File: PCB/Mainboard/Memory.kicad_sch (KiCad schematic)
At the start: 10 parts, among them J301 Conn_SIMM72, J302 Conn_SIMM72, U301 74F541, U302 74F541

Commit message: Add files via upload
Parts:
- removed J301, J302: Conn_SIMM72, My_Components:Conn_SIMM72, symbol my_components:Conn_SIMM72
- removed R72: 22, Resistor_SMD:R_0612_1632Metric_Pad1.18x3.40mm_HandSolder, symbol Device:R
- removed RN301, RN302, RN303, RN304, RN305: 22, Resistor_THT:R_Array_SIP8, symbol Device:R_Pack04
- removed U301, U302: 74F541, My_Components:IC_DIP20_300, symbol 74xx:74LS541
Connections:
- no-connect marks 18 -> 0
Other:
- note removed: "DRAM Bank 0/1"
- note removed: "DRAM Bank 2/3"

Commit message: Add files via upload
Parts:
- added C101: 180nF, symbol PCM_Elektuur:C
- added C95: 150nF, symbol PCM_Elektuur:C
- added J15: RAM Module, symbol PC110:RAM_MOD
- added U28, U33: M5M4V16160, symbol PC110:M5M4V16160
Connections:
- new net GND: C101.2 (-), C95.2 (-), J15.10 (GND), J15.27 (GND), J15.36 (GND), J15.55 (GND), U28.26 (GND), U28.45 (GND), U28.50 (GND), U33.26 (GND), U33.45 (GND), U33.50 (GND)
- new net PNET1: C101.1 (+), C95.1 (+), J15.14 (VCC), J15.21 (VCC), J15.5 (VCC), U28.1 (VCC), U28.25 (VCC), U28.6 (VCC), U33.1 (VCC), U33.25 (VCC), U33.6 (VCC)
- no-connect marks 0 -> 10

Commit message: Add files via upload
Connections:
- net CPU_D0: now reaches J15.1 (D0)
- net CPU_D0: now also U28.2 (DQ0)
- net RAM_A11: now reaches J15.15 (A11)
- net RAM_A11: now also U28.19 (A11), U33.19 (A11)
- net RAM_A10: now reaches J15.16 (A10)
- net RAM_A10: now also U28.20 (A10), U33.20 (A10)
- net RAM_A0: now reaches J15.17 (A0)
- net RAM_A0: now also U28.21 (A0), U33.21 (A0)
- net RAM_A1: now reaches J15.18 (A1)
- net RAM_A1: now also U28.22 (A1), U33.22 (A1)
- net RAM_A2: now reaches J15.19 (A2)
- net RAM_A2: now also U28.23 (A2), U33.23 (A2)
- net CPU_D1: now reaches J15.2 (D1)
- net CPU_D1: now also U28.3 (DQ1)
- net RAM_A3: now reaches J15.20 (A3)
- net RAM_A3: now also U28.24 (A3), U33.24 (A3)
- net CPU_D16: now reaches J15.22 (D16)
- net CPU_D16: now also U33.2 (DQ0)
- net CPU_D17: now reaches J15.23 (D17)
- net CPU_D17: now also U33.3 (DQ1)
- net CPU_D18: now reaches J15.24 (D18)
- net CPU_D18: now also U33.4 (DQ2)
- net CPU_D19: now reaches J15.25 (D19)
- net CPU_D19: now also U33.5 (DQ3)
- net CPU_D21: now reaches J15.28 (D21)
- net CPU_D21: now also U33.8 (DQ5)
- net CPU_D22: now reaches J15.29 (D22)
- net CPU_D22: now also U33.9 (DQ6)
- net CPU_D2: now reaches J15.3 (D2)
- net CPU_D2: now also U28.4 (DQ2)
- net CPU_D23: now reaches J15.30 (D23)
- net CPU_D23: now also U33.10 (DQ7)
- net CPU_D24: now reaches J15.32 (D24)
- net CPU_D24: now also U33.41 (DQ8)
- net CPU_D25: now reaches J15.33 (D25)
- net CPU_D25: now also U33.42 (DQ9)
- net CPU_D26: now reaches J15.34 (D26)
- net CPU_D26: now also U33.43 (DQ10)
- net CPU_D27: now reaches J15.35 (D27)
- net CPU_D27: now also U33.44 (DQ11)
- net CPU_D28: now reaches J15.37 (D28)
- net CPU_D28: now also U33.46 (DQ12)
- net CPU_D29: now reaches J15.38 (D29)
- net CPU_D29: now also U33.47 (DQ13)
- net CPU_D30: now reaches J15.39 (D30)
- net CPU_D30: now also U33.48 (DQ14)
- net CPU_D3: now reaches J15.4 (D3)
- net CPU_D3: now also U28.5 (DQ3)
- net CPU_D31: now reaches J15.40 (D31)
- net CPU_D31: now also U33.49 (DQ15)
- net RAM_A4: now reaches J15.41 (A4)
- net RAM_A4: now also U28.27 (A4), U33.27 (A4)
- net RAM_A5: now reaches J15.42 (A5)
- net RAM_A5: now also U28.28 (A5), U33.28 (A5)
- net RAM_A6: now reaches J15.43 (A6)
- net RAM_A6: now also U28.29 (A6), U33.29 (A6)
- net RAM_A7: now reaches J15.44 (A7)
- net RAM_A7: now also U28.30 (A7), U33.30 (A7)
- net RAM_A8: now reaches J15.45 (A8)
- net RAM_A8: now also U28.31 (A8), U33.31 (A8)
- net RAM_A9: now reaches J15.46 (A9)
- net RAM_A9: now also U28.32 (A9), U33.32 (A9)
- net CPU_D8: now reaches J15.51 (D8)
- net CPU_D8: now also U28.41 (DQ8)
- net CPU_D9: now reaches J15.52 (D9)
- net CPU_D9: now also U28.42 (DQ9)
- net CPU_D10: now reaches J15.53 (D10)
- net CPU_D10: now also U28.43 (DQ10)
- net CPU_D11: now reaches J15.54 (D11)
- net CPU_D11: now also U28.44 (DQ11)
- net CPU_D12: now reaches J15.56 (D12)
- net CPU_D12: now also U28.46 (DQ12)
- net CPU_D13: now reaches J15.57 (D13)
- net CPU_D13: now also U28.47 (DQ13)
- net CPU_D14: now reaches J15.58 (D14)
- net CPU_D14: now also U28.48 (DQ14)
- net CPU_D15: now reaches J15.59 (D15)
- net CPU_D15: now also U28.49 (DQ15)
- net CPU_D4: now reaches J15.6 (D4)
- net CPU_D4: now also U28.7 (DQ4)
- net CPU_D5: now reaches J15.7 (D5)
- net CPU_D5: now also U28.8 (DQ5)
- net CPU_D6: now reaches J15.8 (D6)
- net CPU_D6: now also U28.9 (DQ6)
- net CPU_D7: now reaches J15.9 (D7)
- net CPU_D7: now also U28.10 (DQ7)
- net CPU_D20: now reaches U33.7 (DQ4)
- net CPU_D20: now also J15.27 (GND)
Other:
- moved on the sheet: C101, C95, J15, U28, U33

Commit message: Add files via upload
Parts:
- added R101, R103, R106, R154, R159, R261, R272, R274: 33, symbol Device:R
- added R102, R105, R148, R158, R94: 470k, symbol Device:R
- added RA5: 470k, symbol Device:R_Pack04
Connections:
- net CPU_D10: now also U28.37 (DQ10); no longer U28.43 (DQ10)
- net CPU_D11: now also U28.38 (DQ11); no longer U28.44 (DQ11)
- net CPU_D12: now also U28.40 (DQ12); no longer U28.46 (DQ12)
- net CPU_D13: now also U28.41 (DQ13); no longer U28.47 (DQ13)
- net CPU_D14: now also U28.42 (DQ14); no longer U28.48 (DQ14)
- net CPU_D15: now also U28.43 (DQ15); no longer U28.49 (DQ15)
- net CPU_D24: now also U33.35 (DQ8); no longer U33.41 (DQ8)
- net CPU_D25: now also U33.36 (DQ9); no longer U33.42 (DQ9)
- net CPU_D26: now also U33.37 (DQ10); no longer U33.43 (DQ10)
- net CPU_D27: now also U33.38 (DQ11); no longer U33.44 (DQ11)
- net CPU_D28: now also U33.40 (DQ12); no longer U33.46 (DQ12)
- net CPU_D29: now also U33.41 (DQ13); no longer U33.47 (DQ13)
- net CPU_D30: now also U33.42 (DQ14); no longer U33.48 (DQ14)
- net CPU_D31: now also U33.43 (DQ15); no longer U33.49 (DQ15)
- net CPU_D8: now also U28.35 (DQ8); no longer U28.41 (DQ8)
- net CPU_D9: now also U28.36 (DQ9); no longer U28.42 (DQ9)
- net GND: now also U28.23 (GND), U28.30 (OE#), U28.39 (GND), U28.44 (GND), U33.23 (GND), U33.30 (OE#), U33.39 (GND), U33.44 (GND); no longer U28.26 (GND), U28.45 (GND), U28.50 (GND), U33.26 (GND), U33.45 (GND), U33.50 (GND)
- net PNET1: now also U28.22 (VCC), U33.22 (VCC), R102.2, R105.2, R148.2, R158.2, R94.2, RA5.5 (R4.2), RA5.6 (R3.2), RA5.7 (R2.2), RA5.8 (R1.2); no longer U28.25 (VCC), U33.25 (VCC)
- net RAM_A0: now also U28.18 (A0), U33.18 (A0); no longer U28.21 (A0), U33.21 (A0)
- net RAM_A1: now also U28.19 (A1), U33.19 (A1); no longer U28.22 (A1), U33.22 (A1)
- net RAM_A10: now also U28.17 (A10), U33.17 (A10); no longer U28.20 (A10), U33.20 (A10)
- net RAM_A11: now also U28.16 (A11), U33.16 (A11); no longer U28.19 (A11), U33.19 (A11)
- net RAM_A2: now also U28.20 (A2), U33.20 (A2); no longer U28.23 (A2), U33.23 (A2)
- net RAM_A3: now also U28.21 (A3), U33.21 (A3); no longer U28.24 (A3), U33.24 (A3)
- net RAM_A4: now also U28.24 (A4), U33.24 (A4); no longer U28.27 (A4), U33.27 (A4)
- net RAM_A5: now also U28.25 (A5), U33.25 (A5); no longer U28.28 (A5), U33.28 (A5)
- net RAM_A6: now also U28.26 (A6), U33.26 (A6); no longer U28.29 (A6), U33.29 (A6)
- net RAM_A7: now also U28.27 (A7), U33.27 (A7); no longer U28.30 (A7), U33.30 (A7)
- net RAM_A8: now also U28.28 (A8), U33.28 (A8); no longer U28.31 (A8), U33.31 (A8)
- net RAM_A9: now also U28.29 (A9), U33.29 (A9); no longer U28.32 (A9), U33.32 (A9)
- net at J15.11 (RAS2): now also R102.1, R103.2
- net LCASU#: now reaches J15.12 (LCASU#)
- net LCASU#: now also U28.32 (LCAS#), R274.2, RA5.4 (R4.1)
- net UCASU#: now reaches J15.13 (UCASU#)
- net UCASU#: now also U28.31 (UCAS#), R261.2, RA5.3 (R3.1)
- net RAM_ID1: now reaches J15.31 (ID1)
- net RAM_ID1: now also R148.1
- net UCASL#: now reaches J15.47 (UCASL#)
- net UCASL#: now also U33.31 (UCAS#), R159.2, RA5.1 (R1.1)
- net LCASL#: now reaches J15.48 (LCASL#)
- net LCASL#: now also U33.32 (LCAS#), R272.2, RA5.2 (R2.1)
- net at J15.49 (RAS3): now also R106.2, R94.1
- net RAMWE#: now reaches J15.50 (WE#)
- net RAMWE#: now also U28.14 (W#), U33.14 (W#), R154.2
- net RAM_ID0: now reaches J15.60 (ID0)
- net RAM_ID0: now also R158.1
- net at U33.15 (RAS#): now also U28.15 (RAS#), R101.2, R105.1
- new net RAM_LCASL#: R272.1
- new net RAM_LCASU#: R274.1
- new net RAM_RAMWE#: R154.1
- new net RAM_RAS1: R101.1
- new net RAM_RAS2: R103.1
- new net RAM_RAS3: R106.1
- new net RAM_UCASL#: R159.1
- new net RAM_UCASU#: R261.1
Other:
- moved on the sheet: C101, C95, J15, U28, U33

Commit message: Add files via upload
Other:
- company: (none) -> Recreated by: Ahmad Byagowi
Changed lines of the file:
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@@
 	(title_block
 		(title "PC110")
+		(company "Recreated by: Ahmad Byagowi")
 	)
 	(junction

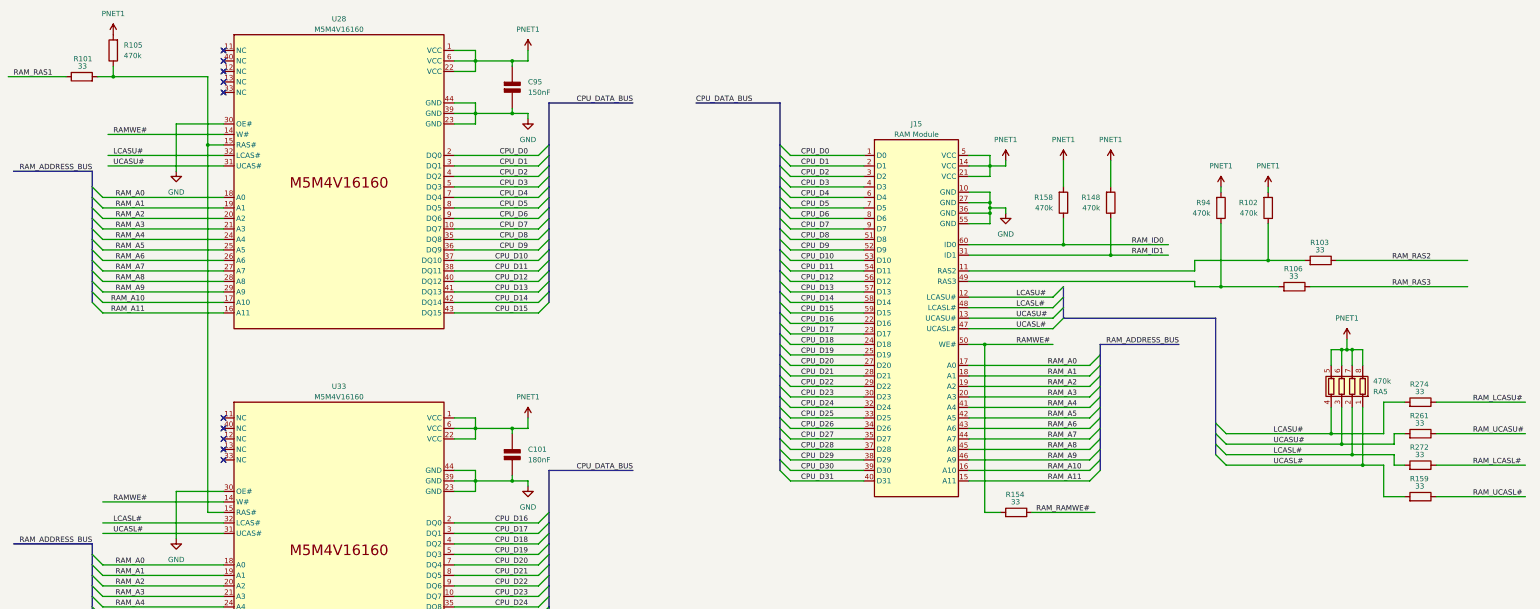
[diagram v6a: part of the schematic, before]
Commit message: Add part numbers to some SMT parts
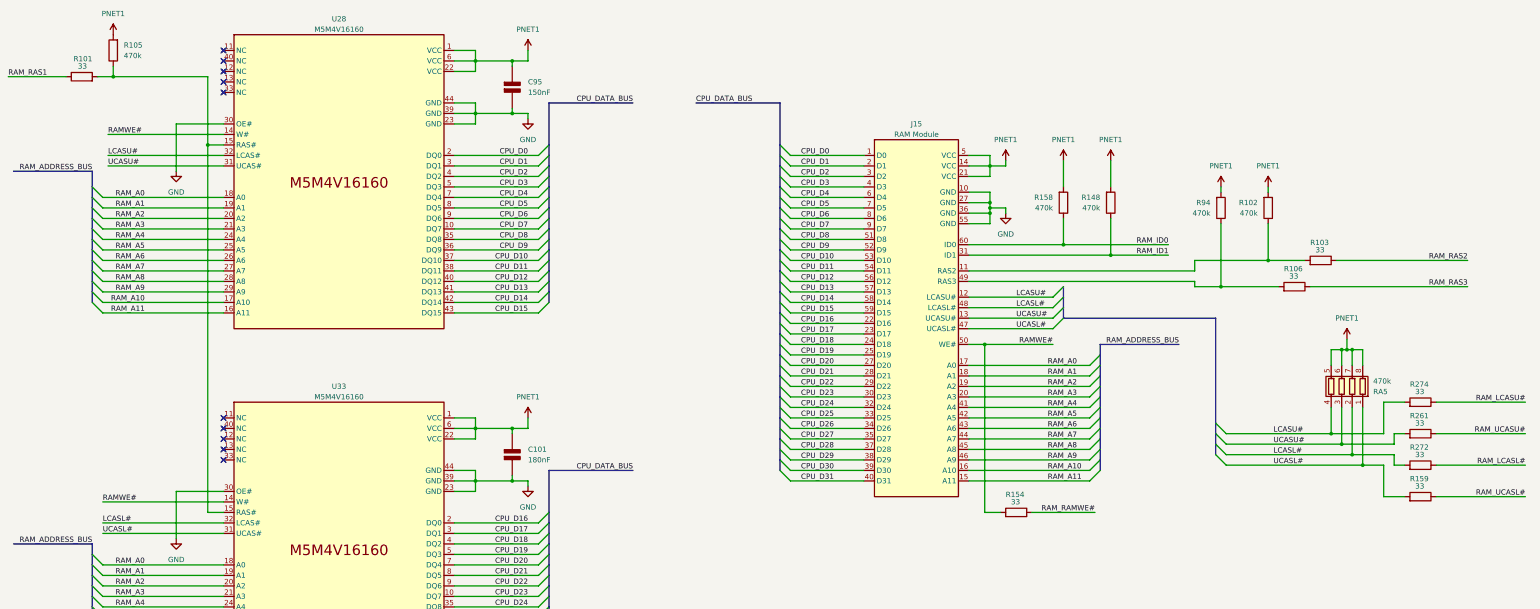
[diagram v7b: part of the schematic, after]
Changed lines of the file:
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@@
 	)
 	(label "LCASU#"
-		(at 57.15 93.98 0)
+		(at 55.88 93.98 0)
 		(effects
 			(font
@@
 	)
 	(label "RAM_ID0"
-		(at 303.53 115.57 0)
-		(effects
-			(font
-				(size 1.27 1.27)
-			)
-			(justify left bottom)
+		(at 312.42 115.57 180)
+		(effects
+			(font
+				(size 1.27 1.27)
+			)
+			(justify right bottom)
 		)
 	)
@@
 	)
 	(label "RAM_RAS1"
-		(at 33.02 74.93 0)
+		(at 31.75 74.93 0)
 		(effects
 			(font
@@
 	)
 	(label "RAM_LCASL#"
-		(at 386.08 168.91 0)
-		(effects
-			(font
-				(size 1.27 1.27)
-			)
-			(justify left bottom)
+		(at 398.78 168.91 180)
+		(effects
+			(font
+				(size 1.27 1.27)
+			)
+			(justify right bottom)
 		)
 	)
@@
 	)
 	(label "RAMWE#"
-		(at 57.15 177.8 0)
+		(at 54.61 177.8 0)
 		(effects
 			(font
@@
 	)
 	(label "RAM_RAMWE#"
-		(at 293.37 180.34 180)
+		(at 294.64 180.34 180)
 		(effects
 			(font
@@
 	)
 	(label "LCASL#"
-		(at 57.15 182.88 0)
+		(at 54.61 182.88 0)
 		(effects
 			(font
@@
 	)
 	(label "RAM_RAS2"
-		(at 375.92 119.38 180)
+		(at 384.81 119.38 180)
 		(effects
 			(font
@@
 	)
 	(label "RAM_UCASL#"
-		(at 386.08 176.53 0)
-		(effects
-			(font
-				(size 1.27 1.27)
-			)
-			(justify left bottom)
+		(at 398.78 176.53 180)
+		(effects
+			(font
+				(size 1.27 1.27)
+			)
+			(justify right bottom)
 		)
 	)
@@
 	)
 	(label "RAM_RAS3"
-		(at 375.92 125.73 180)
+		(at 384.81 125.73 180)
 		(effects
 			(font
@@
 	)
 	(label "UCASU#"
-		(at 57.15 96.52 0)
+		(at 55.88 96.52 0)
 		(effects
 			(font
@@
 	)
 	(label "RAMWE#"
-		(at 275.59 139.7 0)
-		(effects
-			(font
-				(size 1.27 1.27)
-			)
-			(justify left bottom)
+		(at 284.48 139.7 180)
+		(effects
+			(font
+				(size 1.27 1.27)
+			)
+			(justify right bottom)
 		)
 	)
 	(label "RAM_ID1"
-		(at 303.53 118.11 0)
-		(effects
-			(font
-				(size 1.27 1.27)
-			)
-			(justify left bottom)
+		(at 312.42 118.11 180)
+		(effects
+			(font
+				(size 1.27 1.27)
+			)
+			(justify right bottom)
 		)
 	)
@@
 	)
 	(label "UCASL#"
-		(at 57.15 185.42 0)
+		(at 54.61 185.42 0)
 		(effects
 			(font
@@
 	)
 	(label "RAMWE#"
-		(at 57.15 88.9 0)
+		(at 55.88 88.9 0)
 		(effects
 			(font
@@
 	)
 	(label "RAM_LCASU#"
-		(at 386.08 153.67 0)
-		(effects
-			(font
-				(size 1.27 1.27)
-			)
-			(justify left bottom)
+		(at 398.78 153.67 180)
+		(effects
+			(font
+				(size 1.27 1.27)
+			)
+			(justify right bottom)
 		)
 	)
@@
 	)
 	(label "RAM_UCASU#"
-		(at 386.08 161.29 0)
-		(effects
-			(font
-				(size 1.27 1.27)
-			)
-			(justify left bottom)
-		)
-	)
+		(at 398.78 161.29 180)
+		(effects
+			(font
+				(size 1.27 1.27)
+			)
+			(justify right bottom)
+		)
+	)

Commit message: Add files via upload
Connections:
- net RAM_RAS1 renamed RAM_RAS0
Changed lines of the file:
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@@
 		)
 	)
-	(label "RAM_RAS1"
+	(label "RAM_RAS0"
 		(at 31.75 74.93 0)
 		(effects
